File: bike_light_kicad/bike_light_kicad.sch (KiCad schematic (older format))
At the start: 2 parts

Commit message: added basic SEPIC topology, and PWM controller to schem
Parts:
- added C? (x5): C, symbol Device:C
- added D? (x6): LED, symbol Device:LED
- added D?: D_Schottky, symbol Device:D_Schottky
- added L? (x2): L, symbol Device:L
- added R? (x4): R, symbol Device:R
- added U?: LM3410, symbol Manual_Library:LM3410
- added U?: TLC59711PWPR, digikey-footprints:TSSOP-20-1EP_W4.4mm, symbol Digikey_PMIC_LED:TLC59711PWPR
- added U?: LM2621, symbol Manual_Library:LM2621
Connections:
- net labels added: +5V, GND
- wire segments 0 -> 59

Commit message: Schematic organization, SPMS PNs, Charge controller IC symbol, USBC connections
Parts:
- removed BT?: Battery_Cell, symbol Device:Battery_Cell
- removed C?: C, symbol Device:C
- removed L?: L, symbol Device:L
- removed U?: LM3410, symbol Manual_Library:LM3410
- added BT?: Battery_Cell, symbol Device:Battery_Cell
- added C? (x3): 22uF, symbol Device:C
- added C? (x5): .1uF, symbol Device:C
- added D?: LED, symbol Device:LED
- added J?: 12401832E402A, digikey-footprints:USB-C_Female_12401X, symbol Digikey_USB_CON:12401832E402A
- added J?: AVR-ISP-6, symbol Connector:AVR-ISP-6
- added L?: 22u, symbol Device:L
- added R? (x6): R, symbol Device:R
- added U?: ATtiny85-20SU, Package_SO:SOIJ-8_5.3x5.3mm_P1.27mm, symbol MCU_Microchip_ATtiny:ATtiny85-20SU
- added U?: bq21040, symbol Manual_Library:bq21040
- added U? (x2): CSD16406Q3, symbol Manual_Library:CSD16406Q3
- C?: value C -> 22uF
- C?: value C -> 4.7u
- L?: value L -> 22u
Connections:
- net labels added: +BATT, Cout, Dout, GND1, VBUS
- wire segments 59 -> 131
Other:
- note added: "Charge Controller\n"
- note added: "LED Driver"
- note added: "Protection IC"
- note added: "SEPIC SMPS"
- note added: "USBC Connector"
- note added: "uC"
- moved on the sheet: C?, D?, L?, R?, U?

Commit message: component defs
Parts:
- removed C?: C, symbol Device:C
- added C?: .1uF, symbol Device:C
- added R?: 10k, symbol Device:R
- C?: value C -> 39pF
- R?: value R -> 500
- R?: value R -> 300k
- R?: value R -> 150k
- R?: value R -> 67.4k
- R? (x2): value R -> 5.1k
- R?: value R -> 150
- R?: value R -> 330
- gave numbers to parts that had none: 1
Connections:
- net labels added: +4V
- net labels removed: +5V
- wire segments 131 -> 136
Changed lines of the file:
@@
 P 9850 5800
 F 0 "R?" H 9920 5846 50  0000 L CNN
-F 1 "R" H 9920 5755 50  0000 L CNN
+F 1 "500" H 9920 5755 50  0000 L CNN
 F 2 "" V 9780 5800 50  0001 C CNN
 F 3 "~" H 9850 5800 50  0001 C CNN
@@
 	10300 4900 10550 4900
 $Comp
-L Device:C C?
-U 1 1 5F4A1DE7
-P 9850 6200
-F 0 "C?" H 9965 6246 50  0000 L CNN
-F 1 "C" H 9965 6155 50  0000 L CNN
-F 2 "" H 9888 6050 50  0001 C CNN
-F 3 "~" H 9850 6200 50  0001 C CNN
-	1    9850 6200
-	1    0    0    -1
-$EndComp
-$Comp
 L Device:R R?
 U 1 1 5F4A2351
 P 9050 6350
 F 0 "R?" H 9120 6396 50  0000 L CNN
-F 1 "R" H 9120 6305 50  0000 L CNN
+F 1 "300k" H 9120 6305 50  0000 L CNN
 F 2 "" V 8980 6350 50  0001 C CNN
 F 3 "~" H 9050 6350 50  0001 C CNN
@@
 P 8750 7050
 F 0 "R?" V 8543 7050 50  0000 C CNN
-F 1 "R" V 8634 7050 50  0000 C CNN
+F 1 "150k" V 8634 7050 50  0000 C CNN
 F 2 "" V 8680 7050 50  0001 C CNN
 F 3 "~" H 8750 7050 50  0001 C CNN
@@
 P 8350 7750
 F 0 "R?" H 8280 7704 50  0000 R CNN
-F 1 "R" H 8280 7795 50  0000 R CNN
+F 1 "67.4k" H 8280 7795 50  0000 R CNN
 F 2 "" V 8280 7750 50  0001 C CNN
 F 3 "~" H 8350 7750 50  0001 C CNN
@@
 P 8750 7450
 F 0 "C?" V 9002 7450 50  0000 C CNN
-F 1 "C" V 8911 7450 50  0000 C CNN
+F 1 "39pF" V 8911 7450 50  0000 C CNN
 F 2 "" H 8788 7300 50  0001 C CNN
 F 3 "~" H 8750 7450 50  0001 C CNN
@@
 	1    0    0    -1
 $EndComp
-$Comp
-L power:+5V #PWR?
-U 1 1 5F4ACB39
-P 11600 4900
-F 0 "#PWR?" H 11600 4750 50  0001 C CNN
-F 1 "+5V" H 11615 5073 50  0000 C CNN
-F 2 "" H 11600 4900 50  0001 C CNN
-F 3 "" H 11600 4900 50  0001 C CNN
-	1    11600 4900
-	1    0    0    -1
-$EndComp
 Connection ~ 11000 4900
-$Comp
-L power:+5V #PWR?
-U 1 1 5F4AD2D7
-P 9250 7050
-F 0 "#PWR?" H 9250 6900 50  0001 C CNN
-F 1 "+5V" H 9265 7223 50  0000 C CNN
-F 2 "" H 9250 7050 50  0001 C CNN
-F 3 "" H 9250 7050 50  0001 C CNN
-	1    9250 7050
-	1    0    0    -1
-$EndComp
 Wire Wire Line
 	9250 7050 9000 7050
@@
 	11400 5050 11400 4900
 Connection ~ 11400 4900
-Wire Wire Line
-	11400 4900 11600 4900
-Connection ~ 11600 4900
-Wire Wire Line
-	11600 4900 11800 4900
 $Comp
 L Device:L L?
@@
 P 1850 2450
 F 0 "R?" H 1920 2496 50  0000 L CNN
-F 1 "R" H 1920 2405 50  0000 L CNN
+F 1 "5.1k" H 1920 2405 50  0000 L CNN
 F 2 "" V 1780 2450 50  0001 C CNN
 F 3 "~" H 1850 2450 50  0001 C CNN
@@
 U 1 1 5F4F6664
 P 3450 2150
-F 0 "R?" H 3520 2196 50  0000 L CNN
-F 1 "R" H 3520 2105 50  0000 L CNN
+F 0 "R?" V 3350 2000 50  0000 L CNN
+F 1 "5.1k" V 3350 2200 50  0000 L CNN
 F 2 "" V 3380 2150 50  0001 C CNN
 F 3 "~" H 3450 2150 50  0001 C CNN
@@
 P 8100 2400
 F 0 "R?" H 8170 2446 50  0000 L CNN
-F 1 "R" H 8170 2355 50  0000 L CNN
+F 1 "150" H 8170 2355 50  0000 L CNN
 F 2 "" V 8030 2400 50  0001 C CNN
 F 3 "~" H 8100 2400 50  0001 C CNN
@@
 F 1 "LED" H 8093 2826 50  0000 C CNN
 F 2 "" H 8100 2700 50  0001 C CNN
-F 3 "~" H 8100 2700 50  0001 C CNN
+F 3 "https://optoelectronics.liteon.com/upload/download/DS-22-99-0186/LTST-C190KFKT.PDF" H 8100 2700 50  0001 C CNN
 	1    8100 2700
 	0    1    -1   0
@@
 P 11250 1700
 F 0 "R?" H 11320 1746 50  0000 L CNN
-F 1 "R" H 11320 1655 50  0000 L CNN
+F 1 "330" H 11320 1655 50  0000 L CNN
 F 2 "" V 11180 1700 50  0001 C CNN
 F 3 "~" H 11250 1700 50  0001 C CNN
@@
 	11250 2350 11250 2300
 $Comp
-L Device:R R?
+L Device:R 2.2k
 U 1 1 5F5C8227
 P 11650 2350
-F 0 "R?" H 11720 2396 50  0000 L CNN
+F 0 "2.2k" H 11720 2396 50  0000 L CNN
 F 1 "R" H 11720 2305 50  0000 L CNN
 F 2 "" V 11580 2350 50  0001 C CNN
@@
 	1    0    0    -1
 $EndComp
+$Comp
+L power:GND1 #PWR?
+U 1 1 5F4D53A4
+P 2400 3250
+F 0 "#PWR?" H 2400 3000 50  0001 C CNN
+F 1 "GND1" V 2405 3122 50  0000 R CNN
+F 2 "" H 2400 3250 50  0001 C CNN
+F 3 "" H 2400 3250 50  0001 C CNN
+	1    2400 3250
+	1    0    0    -1
+$EndComp
+$Comp
+L Device:R R?
+U 1 1 5F4D8FB6
+P 8100 1650
+F 0 "R?" H 8170 1696 50  0000 L CNN
+F 1 "10k" H 8170 1605 50  0000 L CNN
+F 2 "" V 8030 1650 50  0001 C CNN
+F 3 "~" H 8100 1650 50  0001 C CNN
+	1    8100 1650
+	-1   0    0    -1
+$EndComp
+$Comp
+L power:GND1 #PWR?
+U 1 1 5F4DA303
+P 8100 1800
+F 0 "#PWR?" H 8100 1550 50  0001 C CNN
+F 1 "GND1" H 8105 1627 50  0000 C CNN
+F 2 "" H 8100 1800 50  0001 C CNN
+F 3 "" H 8100 1800 50  0001 C CNN
+	1    8100 1800
+	-1   0    0    -1
+$EndComp
+Wire Wire Line
+	7650 2050 7650 1400
+Wire Wire Line
+	7650 1400 8100 1400
+Wire Wire Line
+	8100 1400 8100 1500
+$Comp
+L power:+4V #PWR?
+U 1 1 5F4EE638
+P 11600 4900
+F 0 "#PWR?" H 11600 4750 50  0001 C CNN
+F 1 "+4V" H 11615 5073 50  0000 C CNN
+F 2 "" H 11600 4900 50  0001 C CNN
+F 3 "" H 11600 4900 50  0001 C CNN
+	1    11600 4900
+	1    0    0    -1
+$EndComp
+Wire Wire Line
+	11400 4900 11600 4900
+Connection ~ 11600 4900
+Wire Wire Line
+	11600 4900 11800 4900
+$Comp
+L power:+4V #PWR?
+U 1 1 5F4EEFD1
+P 9250 7050
+F 0 "#PWR?" H 9250 6900 50  0001 C CNN
+F 1 "+4V" H 9265 7223 50  0000 C CNN
+F 2 "" H 9250 7050 50  0001 C CNN
+F 3 "" H 9250 7050 50  0001 C CNN
+	1    9250 7050
+	1    0    0    -1
+$EndComp
+Wire Wire Line
+	8950 5800 9050 5800
+Wire Wire Line
+	9050 5800 9050 5950
+$Comp
+L Device:C C?
+U 1 1 5F4FE39A
+P 9850 6200
+F 0 "C?" H 9965 6246 50  0000 L CNN
+F 1 ".1uF" H 9965 6155 50  0000 L CNN
+F 2 "" H 9888 6050 50  0001 C CNN
+F 3 "399-1099-1-ND" H 9850 6200 50  0001 C CNN
+	1    9850 6200
+	1    0    0    -1
+$EndComp

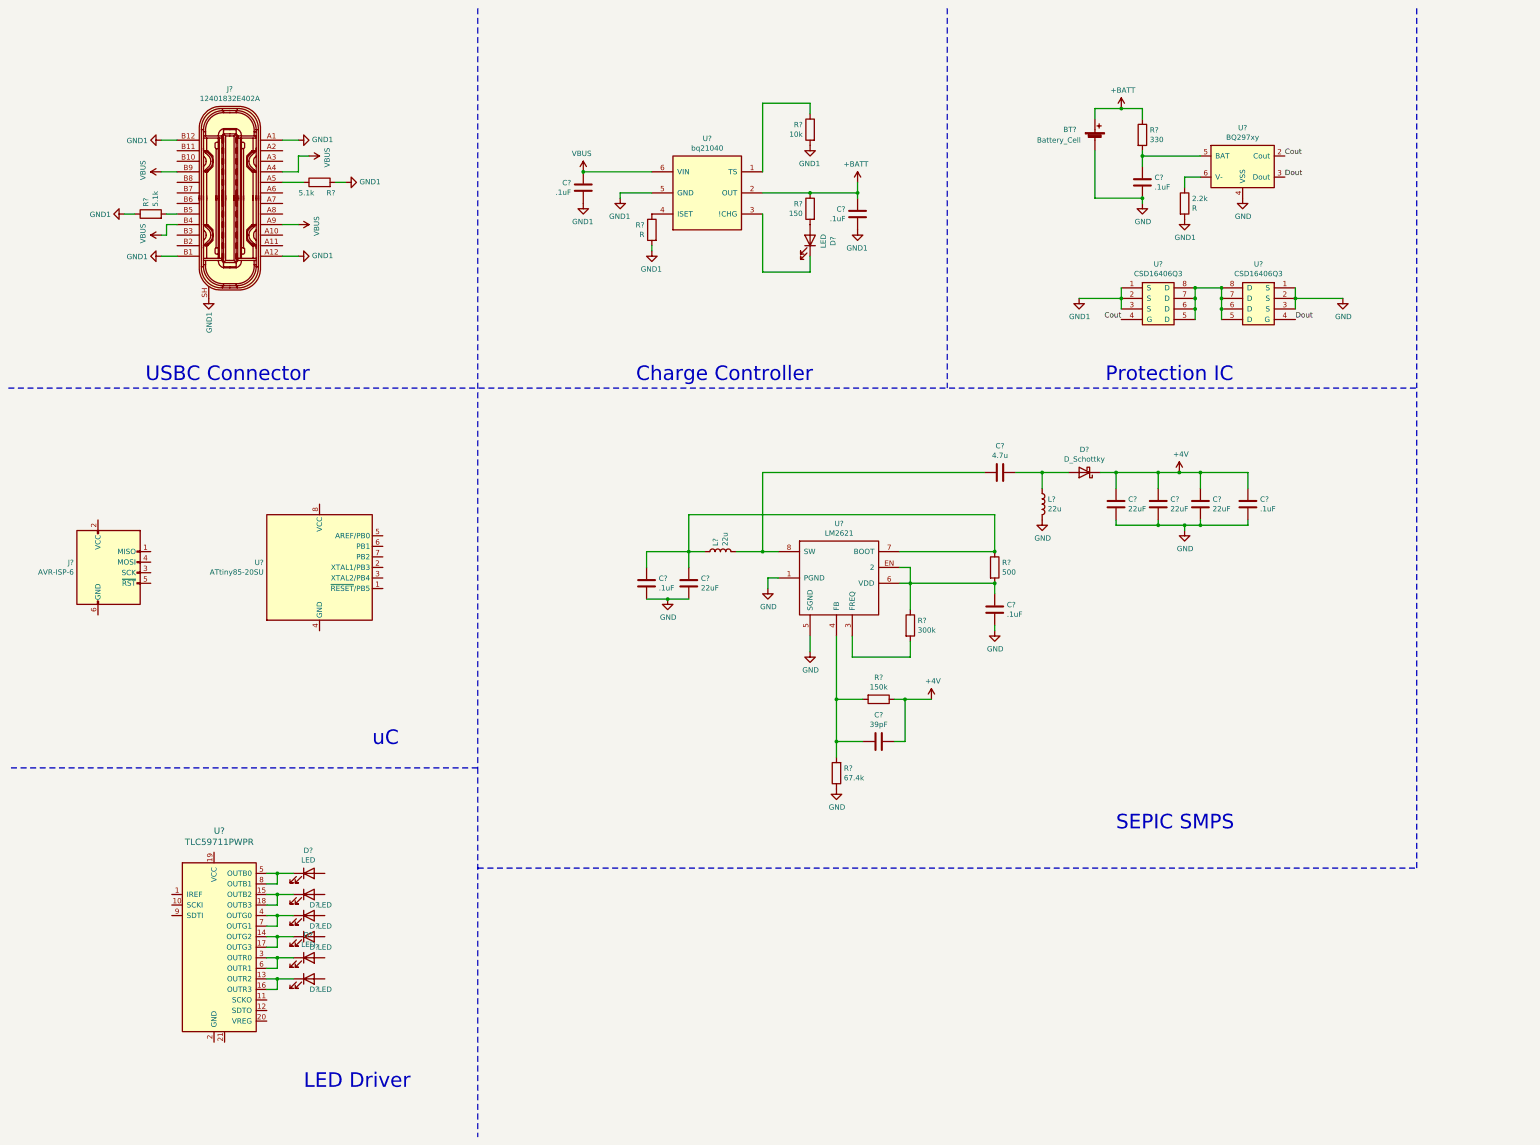
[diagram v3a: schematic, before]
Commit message: Linear reg added, ground error fixed, LED connections, button input, power switch
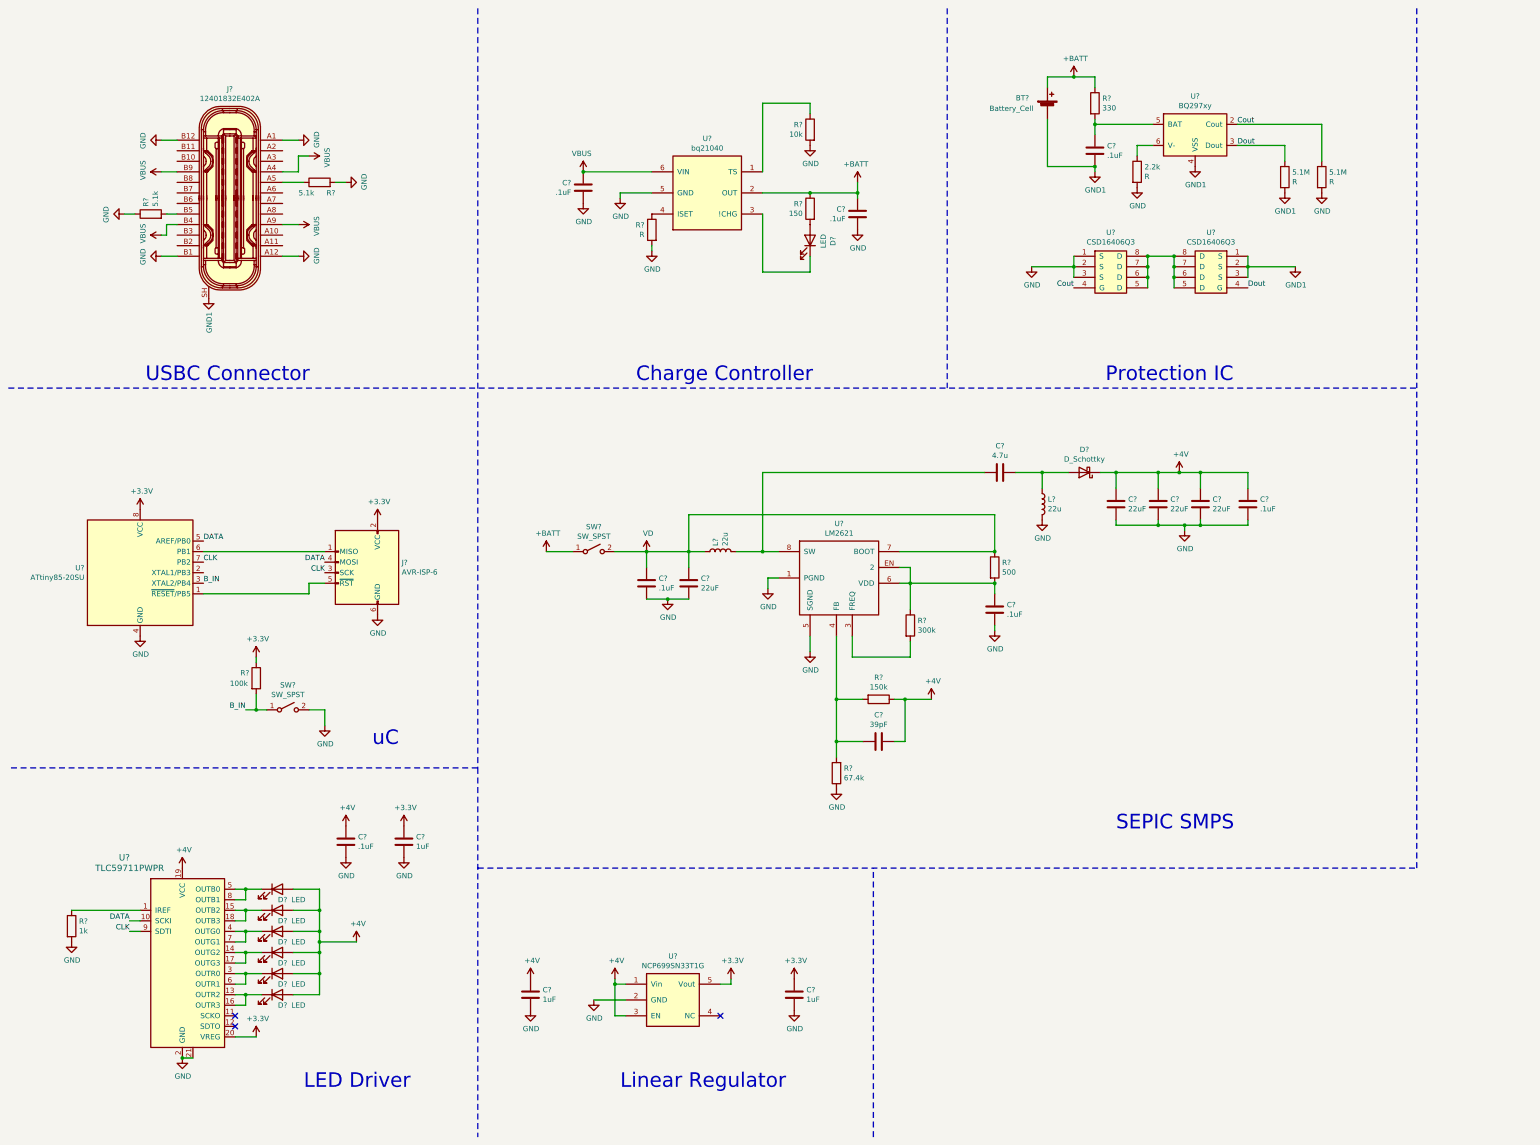
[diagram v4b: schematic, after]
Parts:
- added 5.1M (x2): R, symbol Device:R
- added C?: .1uF, symbol Device:C
- added C? (x3): 1uF, symbol Device:C
- added R?: 1k, symbol Device:R
- added R?: 100k, symbol Device:R
- added SW? (x2): SW_SPST, symbol Switch:SW_SPST
- added U?: NCP699SN33T1G, symbol Manual_Library:NCP699SN33T1G
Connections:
- net +4V: now also D?.2 (A), D?.2 (A), D?.2 (A), D?.2 (A), D?.2 (A), D?.2 (A), U?.19 (VCC), C?.1, C?.1, U?.1 (Vin), U?.3 (EN)
- net +BATT: now also SW?.1 (A)
- net Cout: now also 5.1M.1
- net Dout: now also 5.1M.1
- net GND: now also 2.2k.2, C?.2, C?.2, J?.6 (GND), J?.A1, J?.A12, J?.B1, J?.B12, R?.1, R?.2, R?.2, R?.2, U?.1 (S), U?.2 (GND), U?.2 (S), U?.21, U?.3 (S), U?.4 (GND), U?.5 (GND), 5.1M.2, C?.2, C?.2, C?.2, C?.2, R?.2, SW?.2 (B), U?.2 (GND); no longer BT?.2 (-), C?.2, U?.1 (S), U?.2 (S), U?.3 (S), U?.4 (VSS)
- net GND1: now also BT?.2 (-), C?.2, U?.1 (S), U?.2 (S), U?.3 (S), U?.4 (VSS), 5.1M.2; no longer 2.2k.2, C?.2, C?.2, J?.A1, J?.A12, J?.B1, J?.B12, R?.1, R?.2, R?.2, R?.2, U?.1 (S), U?.2 (S), U?.3 (S), U?.5 (GND)
- net at U?.1 (IREF): now also R?.1
- net DATA: now reaches U?.10 (SCKI)
- net DATA: now also J?.4 (MOSI), U?.5 (AREF/PB0)
- net +3V3: now reaches U?.20 (VREG)
- net +3V3: now also J?.2 (VCC), U?.8 (VCC), C?.1, C?.1, R?.1, U?.5 (Vout)
- net CLK: now reaches U?.9 (SDTI)
- net CLK: now also J?.3 (SCK), U?.7 (PB2)
- net VD: now reaches C?.1, C?.1, L?.1, R?.1, U?.7 (BOOT)
- net VD: now also SW?.2 (B)
- net at U?.1 (~RESET~/PB5): now also J?.5 (~RST)
- net B_IN: now reaches U?.3 (XTAL2/PB4)
- net B_IN: now also R?.2, SW?.1 (A)
- net at U?.6 (PB1): now also J?.1 (MISO)
- no-connect marks 0 -> 3
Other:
- note added: "Linear Regulator"
- moved on the sheet: 2.2k, BT?, C?, D?, J?, R?, U?
